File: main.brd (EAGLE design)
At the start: 50.8 x 50.8 mm, 91 parts, among them Q1 5.8A/30V/35mΩ, Q2 5.8A/30V/35mΩ, Q3 2.5A/30V/105mΩ, U1 BQ24133_RGY_24, U2 SN65HVD32_D_8

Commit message: First Layout and Schematic
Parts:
- removed 103AT-THERMISTOR: 10k, pinhead:1X02
- removed BATT, VCHG: (no value), pinhead:1X02
- removed C10, C11, C22, C25: 1u, resistor:C0603
- removed C12: 2.2u, resistor:C0603
- removed C13, C14, C16, C18, C21, C5, C8: 100n, resistor:C0603
- removed C15, C19: 10u, resistor:C0603
- removed C17: 47n, resistor:C0603
- removed C4: 6.8n, resistor:C0603
- removed CHG-STAT: 2V @ 20mA, adafruit:CHIPLED_0603
- removed D1: BAS70-05, diode:SOT23
- removed GND-JMP, R23: 0, resistor:R0603
- removed IMU: BNO055, BNO055:LGA28R50P4X10_380X520X100
- removed L2: 6.8u, ipc-7351-inductor:INDC2520X220N
- removed Q1, Q2: 5.8A/30V/35mΩ, SparkFun-DiscreteSemi:SOT23-3
- removed Q3: 2.5A/30V/105mΩ, SparkFun-DiscreteSemi:SOT23-3
- removed R1, R22: 100k, resistor:R0603
- removed R10: 2, resistor:R0603
- removed R11, R12: 4.02k, resistor:R0603
- removed R13: 20m, resistor:R0603
- removed R2: 3.8k, resistor:R0603
- removed R26, R29, R38, R39: 1k, resistor:R0603
- removed R27: 10m, resistor:R0603
- removed R33: 13.8k, resistor:R0603
- removed R36: 5.23k, resistor:R0603
- removed R37: 30.1k, resistor:R0603
- removed R4, R6: 10k, resistor:R0603
- removed R42: 64.9, resistor:R0603
- removed R7: 10, resistor:R0603
- removed R8: 1M, resistor:R0603
- removed R9: 113k, resistor:R0603
- removed U1: BQ24133_RGY_24, BQ24133-UPDATED:RGY24_2P05X3P1
- added VIN: (no value), pinhead:1X02
- GPIO: device pinhead:1X10 -> pinhead:1X08
- moved C7 72.6 mm to (34.5, 11.6), turned to 270 degrees
- moved VDUC 51.8 mm to (38.4, 3.51), turned to 0 degrees
- moved TPS62162-Q1 40.2 mm to (34.5, 14.6), turned to 90 degrees
- moved R3 38.5 mm to (31.6, 14.9), turned to 180 degrees
- moved C6 36.8 mm to (35.8, 17.5)
- moved L1 36.5 mm to (33.8, 18.0)
- moved AIN 36.3 mm to (25.4, 3.81), turned to 180 degrees
- moved R28 35.5 mm to (35.3, 29.3), turned to 90 degrees
- moved C23 35.4 mm to (7.68, 16.1)
- moved S2 34.0 mm to (40.5, 12.1)
- moved GPIO 34.0 mm to (47.0, 26.7), turned to 270 degrees
- moved R25 33.3 mm to (20.3, 6.99), turned to 90 degrees
- moved R24 32.3 mm to (22.9, 6.99), turned to 90 degrees
- moved R21 31.7 mm to (25.4, 6.99), turned to 90 degrees
- moved GND 31.6 mm to (10.7, 9.23)
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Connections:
- removed net *BATDRV: R26.2, U1.19
- removed net AGND: 103AT-THERMISTOR.2, C10.2, C11.2, C14.2, C18.2, C21.2, C25.2, GND-JMP.2, R2.1, R33.1, R37.2, R9.1, U1.25, VCHG.2
- removed net BATT: BATT.1, C16.1, C19.1, C21.1, D1.2, Q3.3, R27.1, U1.15
- removed net GPIO10: GPIO.10
- removed net GPIO9: GPIO.9
- removed net IMU_INT: IMU.14
- removed net N$15: C12.1, R10.1
- removed net N$16: Q1.2, Q2.2, R11.2
- removed net N$17: Q1.1, Q2.1, R12.2
- removed net N$18: IMU.4, R6.2
- removed net N$19: SD.2
- removed net N$21: C10.1, R7.2, U1.4
- removed net N$23: CHG-STAT.A, R42.2
- removed net NRESET: IMU.11, R4.2
- removed net PA16_SER1_I2C_SDA: IMU.20, MCU.25, R38.2
- removed net PA17_SER1_I2C_SCL: IMU.19, MCU.26, R39.2
- removed net PC_ACDRV: R12.1, U1.8
- removed net PC_ACN: C13.2, C14.1, R13.1, R23.2, U1.5
- removed net PC_ACP: C13.1, Q2.3, R13.2, U1.6
- removed net PC_ACSET: R1.1, R33.2, U1.17
- removed net PC_BTST: C17.2, U1.21
- removed net PC_CELL: R29.2, U1.14
- removed net PC_CMSRC: R11.1, U1.7
- removed net PC_ISET: R2.2, R22.1, U1.13
- removed net PC_OVPSET: R8.1, R9.2, U1.18
- removed net PC_PVCC: C15.1, Q3.2, R23.1, S2.2, U1.2, U1.3
- removed net PC_REGN: C22.1, U1.20
- removed net PC_SRP: C16.2, C18.1, L2.2, R27.2, U1.16
- removed net PC_STAT: CHG-STAT.C, U1.9
- removed net PC_SW: C17.1, L2.1, U1.1, U1.24
- removed net PC_TS: 103AT-THERMISTOR.1, R36.2, R37.1, U1.10
- removed net PC_TTC: C25.1, U1.11
- removed net PC_VREF: C11.1, R1.2, R22.2, R29.1, R36.1, R42.1, U1.12
- removed net VIN: D1.1, Q1.3, R10.2, R8.2, VCHG.1
- net 3.3V: no longer C4.1, C5.1, IMU.28, IMU.3, R38.1, R39.1, R4.1, R6.1
- net AIN0: now also MCU.12
- net AIN1: now also MCU.16
- net AIN2: now also MCU.15
- net AIN3: now also MCU.14
- net AIN4: now also MCU.13
- net GND: now also VIN.1; no longer BATT.2, C12.2, C15.2, C19.2, C22.2, C4.2, C5.2, C8.2, GND-JMP.1, IMU.10, IMU.15, IMU.16, IMU.17, IMU.18, IMU.2, IMU.25, IMU.5, IMU.6, U1.22, U1.23
- net GPIO1: now also MCU.32
- net GPIO2: now also MCU.31
- net GPIO3: now also MCU.30
- net GPIO4: now also MCU.29
- net GPIO5: now also MCU.28
- net GPIO6: now also MCU.27
- net GPIO7: now also MCU.26
- net GPIO8: now also MCU.25
- net N$10: now also MCU.34, R41.1; no longer Q3.1, R26.1
- net N$14: now also MCU.33, R28.1; no longer D1.3, R7.1
- net N$9: now also S2.2, VIN.2; no longer C8.1, IMU.9
- net SD_CS: now also MCU.9, SD.2; no longer MCU.1
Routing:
- net GND: track 2.69 -> 195.7 mm, vias 0 -> 10
- net 3.3V: track 0.00 -> 116.5 mm, vias 0 -> 6
- net PB11D_SER4_P3: track 0.00 -> 31.1 mm, vias 0 -> 2
- net SWD_NRES: track 0.00 -> 29.8 mm, vias 0 -> 2
- net PA30_SWCLK: track 0.00 -> 22.7 mm, vias 0 -> 4
- net AIN0: track 0.00 -> 22.5 mm, vias 0 -> 2
- net PB09D_SER4_P1: track 0.00 -> 22.3 mm, vias 0 -> 2
- net SD_CS: track 0.00 -> 21.3 mm, vias 0 -> 2
- net PB08D_SER4_P0: track 0.00 -> 21.3 mm, vias 0 -> 2
- net GPIO1: track 0.00 -> 21.2 mm
- net GPIO2: track 0.00 -> 20.4 mm
- net GPIO3: track 0.00 -> 19.5 mm
- net GPIO8: track 0.00 -> 19.4 mm
- net GPIO4: track 0.00 -> 18.7 mm
- net PC_CMSRC: track 18.6 -> 0.00 mm, vias 1 -> 0
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
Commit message: Added some wires
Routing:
- net 3.3V: track 116.5 -> 123.7 mm, vias 6 -> 8
- net GND: track 195.7 -> 198.5 mm, vias 10 -> 11
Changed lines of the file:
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@@
 <element name="U$4" library="special-drill" package="DRILL_0.1250" value="" x="46.99" y="46.99" locked="yes"/>
 <element name="R41" library="resistor" package="R0603" value="64.9" x="33.02" y="29.2862" rot="R90"/>
-<element name="LED0" library="adafruit" package="CHIPLED_0603" value="2V @ 20mA" x="33.0454" y="32.6263" rot="R180"/>
+<element name="LED0" library="adafruit" package="CHIPLED_0603" value="2V @ 20mA" x="33.0454" y="32.6263" smashed="yes" rot="R180">
+<attribute name="NAME" x="32.6263" y="38.7477" size="1.27" layer="25" rot="R270"/>
+<attribute name="VALUE" x="31.1404" y="33.8963" size="1.27" layer="27" rot="R270"/>
+</element>
 <element name="SD" library="molex-microSD" package="MOLEX_503182-1852" value="503182-1852" x="9.779" y="25.4" locked="yes" rot="R90">
 <attribute name="DESCRIPTION" value="MICRO SD NORMAL ULTRALOWPRO8CKTE" x="9.779" y="25.4" size="1.778" layer="27" rot="R90" display="off"/>
@@
 <element name="R31" library="resistor" package="R0603" value="10k" x="15.0622" y="36.2331" rot="R270"/>
 <element name="R28" library="resistor" package="R0603" value="64.9" x="35.2679" y="29.3116" rot="R90"/>
-<element name="LED1" library="adafruit" package="CHIPLED_0603" value="2V @ 20mA" x="35.2933" y="32.6136" rot="R180"/>
+<element name="LED1" library="adafruit" package="CHIPLED_0603" value="2V @ 20mA" x="35.2933" y="32.6136" smashed="yes" rot="R180">
+<attribute name="NAME" x="34.7853" y="38.862" size="1.27" layer="25" rot="R270"/>
+<attribute name="VALUE" x="33.3883" y="33.8836" size="1.27" layer="27" rot="R270"/>
+</element>
 <element name="TPS62162-Q1" library="TPS62162-Q1" package="DSG0008A" value="" x="34.5186" y="14.6431" rot="R90">
 <attribute name="MANUFACTURER" value="Texas Instruments" x="25.0317" y="14.6431" size="1.778" layer="27" rot="R90" display="off"/>
@@
 <wire x1="23.368" y1="22.5298" x2="24.65" y2="22.5298" width="0.254" layer="1"/>
 <wire x1="24.65" y1="22.5298" x2="24.65" y2="21.15" width="0.254" layer="1"/>
-<wire x1="23.9649" y1="32.4748" x2="21.1328" y2="37.8324" width="0" layer="19" extent="1-1"/>
+<wire x1="23.9649" y1="32.4748" x2="23.4959" y2="32.9438" width="0.254" layer="1"/>
+<wire x1="23.4959" y1="32.9438" x2="23.0632" y2="32.9438" width="0.254" layer="1"/>
+<via x="23.0632" y="32.9438" extent="1-16" drill="0.35"/>
+<wire x1="23.0632" y1="32.9438" x2="23.5204" y2="33.401" width="0.254" layer="16"/>
+<wire x1="23.5204" y1="33.401" x2="23.5204" y2="36.576" width="0.254" layer="16"/>
+<via x="23.5204" y="36.576" extent="1-16" drill="0.35"/>
+<wire x1="23.5204" y1="36.576" x2="23.5204" y2="38.7858" width="0.254" layer="1"/>
+<wire x1="23.5204" y1="38.7858" x2="23.495" y2="38.8112" width="0.254" layer="1"/>
 </signal>
 <signal name="GND">
@@
 <wire x1="17.5881" y1="31.7491" x2="19.7612" y2="31.7491" width="0.508" layer="1"/>
 <via x="17.5881" y="31.7491" extent="1-16" drill="0.35"/>
-<wire x1="17.5881" y1="31.7491" x2="19.9258" y2="34.0868" width="0.508" layer="16"/>
-<wire x1="19.9258" y1="34.0868" x2="22.4028" y2="34.0868" width="0.508" layer="16"/>
 <via x="22.4028" y="34.0868" extent="1-16" drill="0.35"/>
 <wire x1="22.4028" y1="34.0868" x2="23.8769" y2="34.0868" width="0.508" layer="1"/>
@@
 <wire x1="27.9019" y1="27.2796" x2="24.7142" y2="24.0919" width="0.254" layer="16"/>
 <wire x1="24.7142" y1="24.0919" x2="24.7142" y2="23.1902" width="0.254" layer="16"/>
-<wire x1="19.9258" y1="34.0868" x2="21.1328" y2="36.1324" width="0" layer="19" extent="1-16"/>
-<wire x1="34.5186" y1="10.707" x2="34.08205" y2="12.68255" width="0" layer="19" extent="1-16"/>
+<wire x1="17.5881" y1="31.7491" x2="20.0651" y2="31.7491" width="0.254" layer="16"/>
+<wire x1="20.0651" y1="31.7491" x2="22.4028" y2="34.0868" width="0.254" layer="16"/>
+<wire x1="22.4028" y1="34.0868" x2="21.9837" y2="34.0868" width="0.254" layer="16"/>
+<wire x1="21.9837" y1="34.0868" x2="21.1455" y2="34.925" width="0.254" layer="16"/>
+<via x="21.1455" y="34.925" extent="1-16" drill="0.35"/>
+<wire x1="21.1455" y1="34.925" x2="21.1455" y2="36.1197" width="0.254" layer="1"/>
+<wire x1="21.1455" y1="36.1197" x2="21.1328" y2="36.1324" width="0.254" layer="1"/>
+<wire x1="34.08205" y1="12.68255" x2="34.5186" y2="10.707" width="0" layer="19" extent="1-16"/>
 </signal>
 <signal name="VDDCORE">

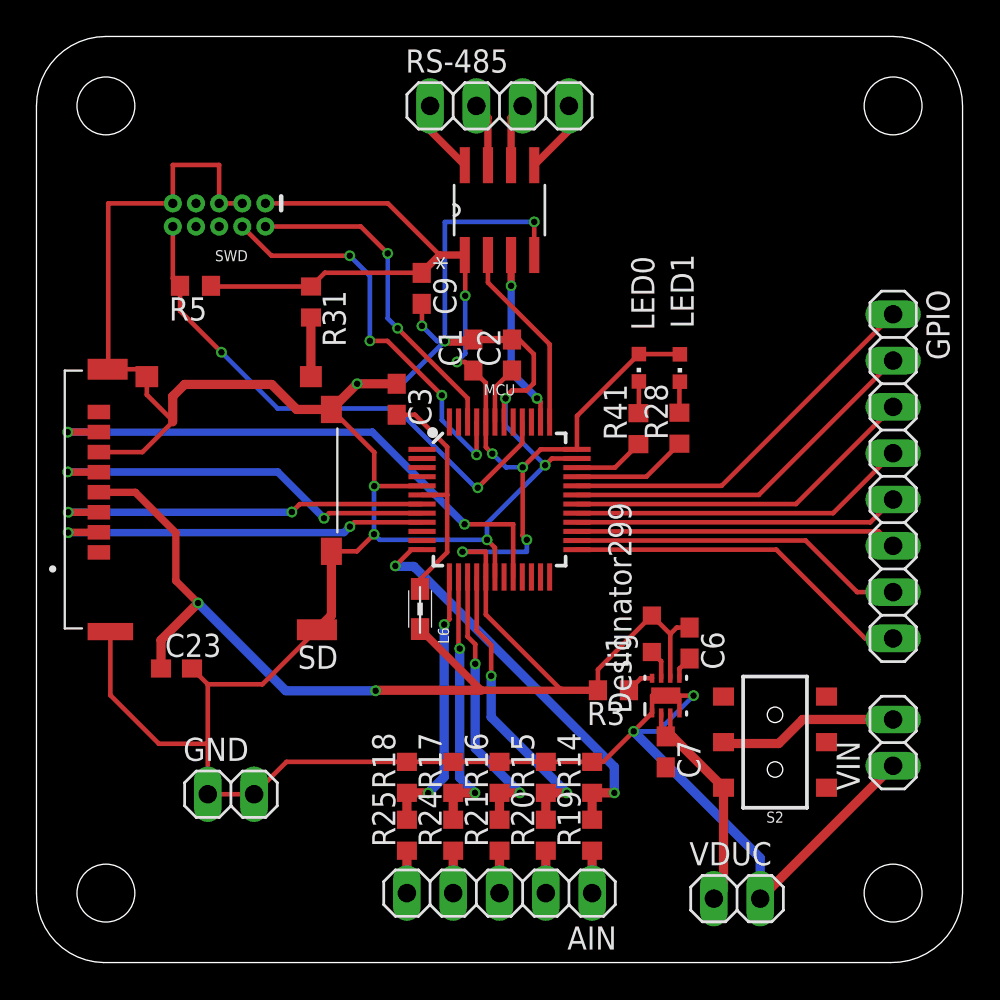
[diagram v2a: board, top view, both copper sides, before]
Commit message: Added gnd pour
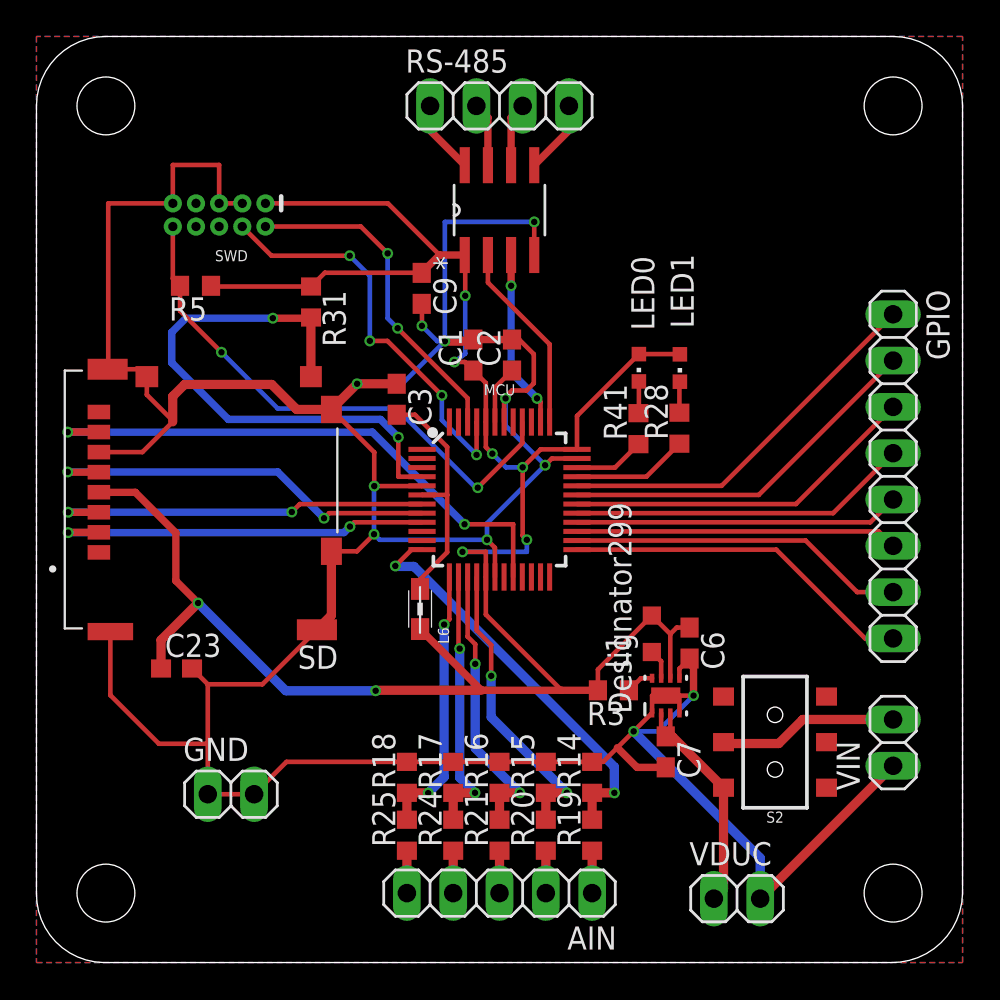
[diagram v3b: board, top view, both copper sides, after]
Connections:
- removed net FB: C6.2, TPS62162-Q1.5
- net GND: now also C6.2, TPS62162-Q1.5
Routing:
- net SD_CD: track 3.25 -> 30.5 mm, vias 0 -> 2
- net GND: track 198.5 -> 205.0 mm
- net FB: track 1.31 -> 0.00 mm
- added copper zone on layer 1, net GND
- added copper zone on layer 16, net GND
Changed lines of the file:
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@@
 <wire x1="24.65" y1="22.5298" x2="24.65" y2="21.15" width="0.254" layer="1"/>
 <wire x1="23.9649" y1="32.4748" x2="23.4959" y2="32.9438" width="0.254" layer="1"/>
-<wire x1="23.4959" y1="32.9438" x2="23.0632" y2="32.9438" width="0.254" layer="1"/>
-<via x="23.0632" y="32.9438" extent="1-16" drill="0.35"/>
-<wire x1="23.0632" y1="32.9438" x2="23.5204" y2="33.401" width="0.254" layer="16"/>
+<wire x1="23.4959" y1="32.9438" x2="22.9235" y2="32.9438" width="0.254" layer="1"/>
+<via x="22.9235" y="32.9438" extent="1-16" drill="0.35"/>
+<wire x1="22.9235" y1="32.9438" x2="23.5204" y2="33.401" width="0.254" layer="16"/>
 <wire x1="23.5204" y1="33.401" x2="23.5204" y2="36.576" width="0.254" layer="16"/>
 <via x="23.5204" y="36.576" extent="1-16" drill="0.35"/>
@@
 <wire x1="27.2796" y1="33.3756" x2="26.4804" y2="34.1748" width="0.254" layer="1"/>
 <via x="32.75805" y="12.68255" extent="1-16" drill="0.35"/>
-<wire x1="31.0855" y1="11.01" x2="32.75805" y2="12.68255" width="0.254" layer="1"/>
+<wire x1="31.0855" y1="11.01" x2="31.8627" y2="11.7872" width="0.254" layer="1"/>
+<wire x1="31.8627" y1="11.7872" x2="32.75805" y2="12.68255" width="0.254" layer="1"/>
 <wire x1="32.75805" y1="12.68255" x2="34.08205" y2="12.68255" width="0.254" layer="16"/>
 <wire x1="34.08205" y1="12.68255" x2="36.0426" y2="14.6431" width="0.254" layer="16"/>
@@
 <wire x1="21.1455" y1="34.925" x2="21.1455" y2="36.1197" width="0.254" layer="1"/>
 <wire x1="21.1455" y1="36.1197" x2="21.1328" y2="36.1324" width="0.254" layer="1"/>
-<wire x1="34.08205" y1="12.68255" x2="34.5186" y2="10.707" width="0" layer="19" extent="1-16"/>
+<polygon width="0.1524" layer="16" isolate="0.381">
+<vertex x="0" y="0"/>
+<vertex x="50.8" y="0"/>
+<vertex x="50.8" y="50.8"/>
+<vertex x="0" y="50.8"/>
+</polygon>
+<polygon width="0.1524" layer="1" isolate="0.381">
+<vertex x="0" y="0"/>
+<vertex x="50.8" y="0"/>
+<vertex x="50.8" y="50.8"/>
+<vertex x="0" y="50.8"/>
+</polygon>
+<contactref element="C6" pad="2"/>
+<contactref element="TPS62162-Q1" pad="5"/>
+<wire x1="35.2686" y1="15.5931" x2="35.2686" y2="16.1179" width="0.254" layer="1"/>
+<wire x1="35.2686" y1="16.1179" x2="35.6929" y2="16.5422" width="0.254" layer="1"/>
+<wire x1="35.6929" y1="16.5422" x2="35.8267" y2="16.676" width="0.254" layer="1"/>
+<wire x1="36.0426" y1="14.6431" x2="36.0426" y2="16.1925" width="0.4064" layer="1"/>
+<wire x1="36.0426" y1="16.1925" x2="35.6929" y2="16.5422" width="0.4064" layer="1"/>
+<wire x1="34.5186" y1="10.707" x2="32.9429" y2="10.707" width="0.4064" layer="1"/>
+<wire x1="32.9429" y1="10.707" x2="31.8627" y2="11.7872" width="0.4064" layer="1"/>
 </signal>
 <signal name="VDDCORE">
@@
 <wire x1="15.054" y1="32.14" x2="15.054" y2="35.3749" width="0.508" layer="1"/>
 <wire x1="15.054" y1="35.3749" x2="15.0622" y2="35.3831" width="0.508" layer="1"/>
-<wire x1="15.054" y1="32.14" x2="21.15" y2="26.65" width="0" layer="19" extent="1-1"/>
+<wire x1="21.15" y1="26.65" x2="19.8501" y2="26.65" width="0.254" layer="1"/>
+<wire x1="19.8501" y1="26.65" x2="19.8501" y2="28.8163" width="0.254" layer="1"/>
+<via x="19.8501" y="28.8163" extent="1-16" drill="0.35"/>
+<wire x1="19.8501" y1="28.8163" x2="18.8722" y2="29.7942" width="0.4064" layer="16"/>
+<wire x1="18.8722" y1="29.7942" x2="10.5283" y2="29.7942" width="0.4064" layer="16"/>
+<wire x1="10.5283" y1="29.7942" x2="7.4168" y2="32.9057" width="0.4064" layer="16"/>
+<wire x1="7.4168" y1="32.9057" x2="7.4168" y2="34.5694" width="0.4064" layer="16"/>
+<wire x1="7.4168" y1="34.5694" x2="8.1915" y2="35.3441" width="0.4064" layer="16"/>
+<wire x1="8.1915" y1="35.3441" x2="12.9667" y2="35.3441" width="0.4064" layer="16"/>
+<via x="12.9667" y="35.3441" extent="1-16" drill="0.35"/>
+<wire x1="12.9667" y1="35.3441" x2="15.0232" y2="35.3441" width="0.4064" layer="1"/>
+<wire x1="15.0232" y1="35.3441" x2="15.0622" y2="35.3831" width="0.4064" layer="1"/>
 </signal>
 <signal name="N$20">
@@
 <wire x1="33.7686" y1="15.5931" x2="33.1563" y2="15.5931" width="0.254" layer="1"/>
 <wire x1="33.1563" y1="15.5931" x2="32.4984" y2="14.9352" width="0.254" layer="1"/>
-</signal>
-<signal name="FB">
-<contactref element="C6" pad="2"/>
-<contactref element="TPS62162-Q1" pad="5"/>
-<wire x1="35.2686" y1="15.5931" x2="35.2686" y2="16.1179" width="0.254" layer="1"/>
-<wire x1="35.2686" y1="16.1179" x2="35.8267" y2="16.676" width="0.254" layer="1"/>
 </signal>
 <signal name="N$9">
@@
 </signal>
 </signals>
+<errors>
+</errors>
 </board>
 </drawing>
